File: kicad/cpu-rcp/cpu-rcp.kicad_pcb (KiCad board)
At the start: 2 copper layers, 86.4 x 63.5 mm, 79 parts, among them P1 RDRAM-EDGE, P5 NINTENDO-64_PINHEAD-25X2, SW1 Reset, U1 9480F, U10 CPU-NUS, U6 PIF-NUS, U7 MX8330, U9 RCP-NUS, X1 14.318MHz

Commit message: Work in progress, updated 3D shapes
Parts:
- added DA1: BAC54, n64:D_SOT-23_AAK, B.Cu at (96.5, 45.7)
- added FIL2: 3.3uH, n64:L_0805, B.Cu at (101.6, 47.0)
- added FIL4: 3.3uH, n64:L_0805, B.Cu at (101.6, 43.2)
- added JOY1: JOY OUT, n64:connector-molex-505110-0492, B.Cu at (105.9, 45.5)
- added R37: 750R, n64:R_0603, B.Cu at (92.0, 62.2)
- added R38: 750R, n64:R_0603, B.Cu at (85.1, 61.0)
- added U8: LC125, n64:ssop-14, B.Cu at (99.1, 58.4)
- moved U6 8.26 mm to (85.1, 52.1)
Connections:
- C144 pad 1: Net-(C144-Pad1) -> GND
- C144 pad 2: GND -> Net-(C144-Pad2)
- DCIN1 pad 4: ENABLE -> +3V3
- R36 pad 1: Net-(C144-Pad1) -> ENABLE
- R36 pad 2: ENABLE -> Net-(C144-Pad2)
- U6 pad 15: Net-(U6-Pad15) -> JOY1_DATA
- U6 pad 17: Net-(U6-Pad17) -> JOY2_DATA
- U7 pad 7: Net-(C144-Pad1) -> Net-(C144-Pad2)

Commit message: Laying around
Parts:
- C123, C127, C128, C5, C6, C7, C8, C9, CC1, CC2, CC3, CC4, CC5, CC6, CC7, CC8, CC9, CP1, CP2, CP3, CP4, CP5, CP6, CR1, CR10, CR11, CR12, CR13, CR14, CR15, CR2, CR3, CR4, CR5, CR6, CR7, CR8, CR9, CU1, CU7, CV1, CV2, R12, R13, R22, R23, R24, R28, R29, R3, R30, R34, R36, R4, SW1: moved to B.Cu
- moved SW1 60.5 mm to (36.8, 27.3), turned to 270 degrees
- moved AUDIO1 56.3 mm to (63.3, 83.5), turned to 0 degrees
- moved C127 54.1 mm to (42.5, 29.8)
- moved CR5 53.9 mm to (94.0, 45.7)
- moved C144 52.8 mm to (106.7, 73.7), turned to 270 degrees
- moved CR4 49.8 mm to (94.5, 52.7)
- moved CR3 48.1 mm to (94.6, 55.9)
- moved C40 47.6 mm to (102.2, 82.5), turned to 90 degrees
- moved C123 45.4 mm to (74.9, 41.9), turned to 180 degrees
- moved CC1 44.9 mm to (35.6, 41.9)
- moved CC5 42.2 mm to (43.2, 41.9)
- moved C128 42.2 mm to (62.9, 48.9), turned to 270 degrees
- moved CC2 40.3 mm to (35.6, 47.0)
- moved U1 38.7 mm to (64.1, 74.3)
- moved CR1 38.1 mm to (87.6, 63.5)
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
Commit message: Laying around
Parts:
- removed AUDIO1: AUDIO OUT, n64:connector-molex-505110-0492
- removed CP1, CP2, CP3, CP4, CP5, CP6, CV1, CV2: 100nF, n64:C_0603
- removed REF** (x4): MountingHole_3.2mm_M3, Mounting_Holes:MountingHole_3.2mm_M3_DIN965
- removed VDAC1: RCP DIGITAL RGB OUT, n64:connector-molex-505110-1092
- removed VIDEO1: VIDEO CLOCK/SYNC, n64:connector-molex-505110-0592
- added ANAUD1: ANALOG AUDIO OUT, n64:connector-molex-505110-0492, F.Cu at (64.1, 84.2)
- added AVSYNC1: VIDEO ENCODER SYNC, n64:connector-molex-505110-0492, F.Cu at (107.3, 35.6)
- added CU6: 100nF, n64:C_0603, B.Cu at (67.2, 29.2)
- added CU8: 100nF, n64:C_0603, B.Cu at (45.7, 36.8)
- added CVR1: 100nF, n64:C_0603, B.Cu at (81.3, 70.5)
- added CVR2: 100nF, n64:C_0603, B.Cu at (88.4, 71.1)
- added CVT1: 10uF, n64:C_1206, B.Cu at (90.2, 78.1)
- added CVT2: 100nF, n64:C_0603, B.Cu at (90.2, 74.9)
- added DVO1: DIGITAL VIDEO OUT, n64:connector-molex-505110-1092, F.Cu at (108.5, 54.1)
- C128, C142, C33, C73: footprint n64:CP_Tantalum_Case-D_EIA-7343-31_Reflow -> n64:C_1206
- JOY1: value JOY OUT -> GAMEPAD
- R12, R13, R36: moved to F.Cu
- moved R34 53.8 mm to (34.3, 33.0)
- moved JOY1 51.4 mm to (30.5, 29.8)
- moved R23 43.2 mm to (56.0, 26.7)
- moved R22 40.6 mm to (61.6, 26.7)
- moved R37 39.2 mm to (75.5, 26.7)
- moved R28 38.4 mm to (104.3, 34.9)
- moved SW1 34.9 mm to (71.8, 27.3)
- moved R38 34.3 mm to (91.4, 27.3)
- moved U8 32.6 mm to (40.6, 36.8), turned to 0 degrees
- moved R12 31.6 mm to (106.7, 78.1)
- moved R3 28.3 mm to (67.4, 37.5)
- moved R13 26.8 mm to (105.4, 64.1), turned to 90 degrees
- moved CR7 26.5 mm to (90.9, 40.0)
- moved R4 26.4 mm to (60.3, 44.5), turned to 270 degrees
- moved CR6 25.3 mm to (94.6, 43.8)
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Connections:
- P5 pad 13: Net-(P5-Pad13) -> (no net)
- P5 pad 38: Net-(P5-Pad38) -> (no net)
- U10 pad 18: Net-(U10-Pad18) -> (no net)
- U10 pad 65: Net-(U10-Pad65) -> (no net)
- U10 pad 74: Net-(U10-Pad74) -> (no net)
- U10 pad 95: Net-(U10-Pad95) -> (no net)
- U6 pad 26: Net-(U6-Pad26) -> (no net)
- U7 pad 3: Net-(U7-Pad3) -> (no net)

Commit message: Work in progress, laying around
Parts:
- moved U8 1.42 mm to (41.3, 35.6)
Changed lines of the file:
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@@
     (links 437)
     (no_connects 431)
-    (area 16.939279 22.98 114.935 102.125001)
+    (area 25.249999 25.249999 111.910001 89.050001)
     (thickness 1.6)
     (drawings 10)
@@
   )
   (module n64:ssop-14 (layer B.Cu)
-    (at 40.64 36.83)
+    (at 41.275 35.56)
     (fp_text reference U8 (at -3.81 -1.27 270) (layer B.SilkS)
       (effects (font (size 1.2065 1.2065) (thickness 0.1016)) (justify left bottom mirror))

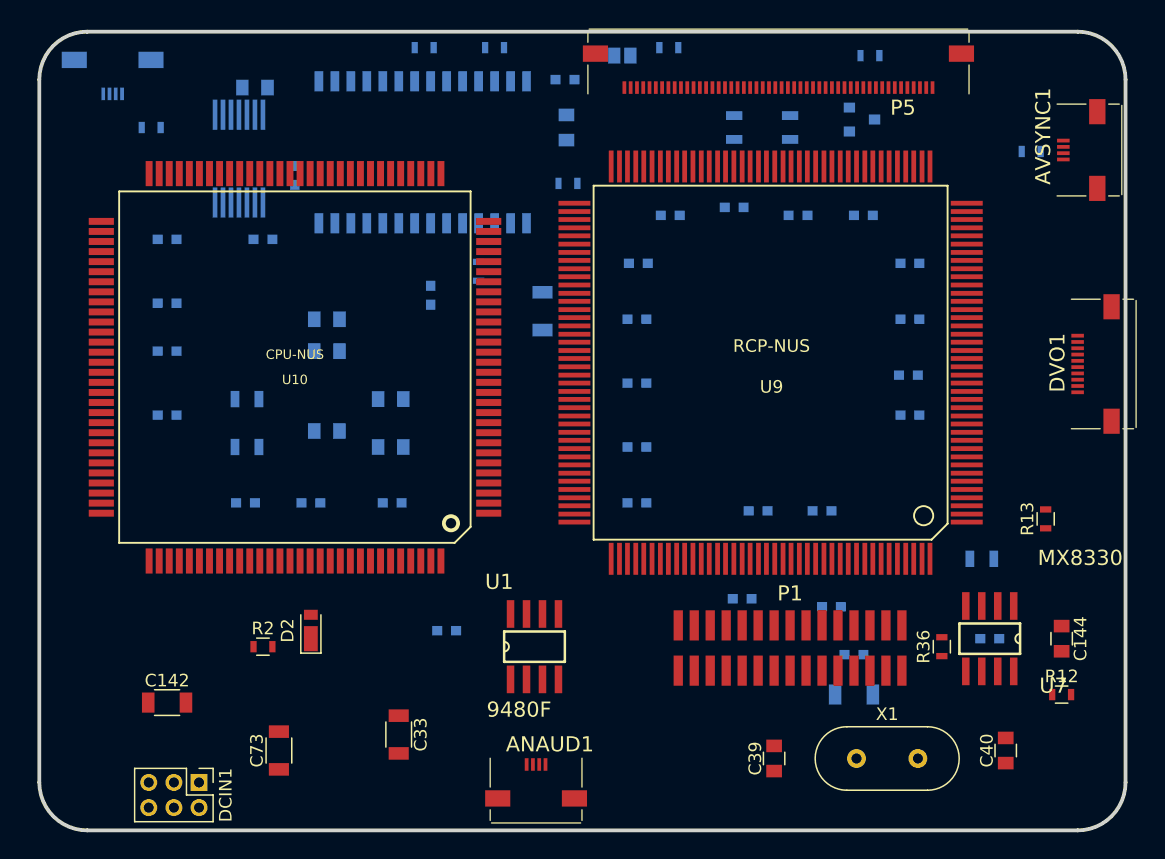
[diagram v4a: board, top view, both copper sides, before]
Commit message: Design Rules set according to my Fab House, switching to 4 layer board
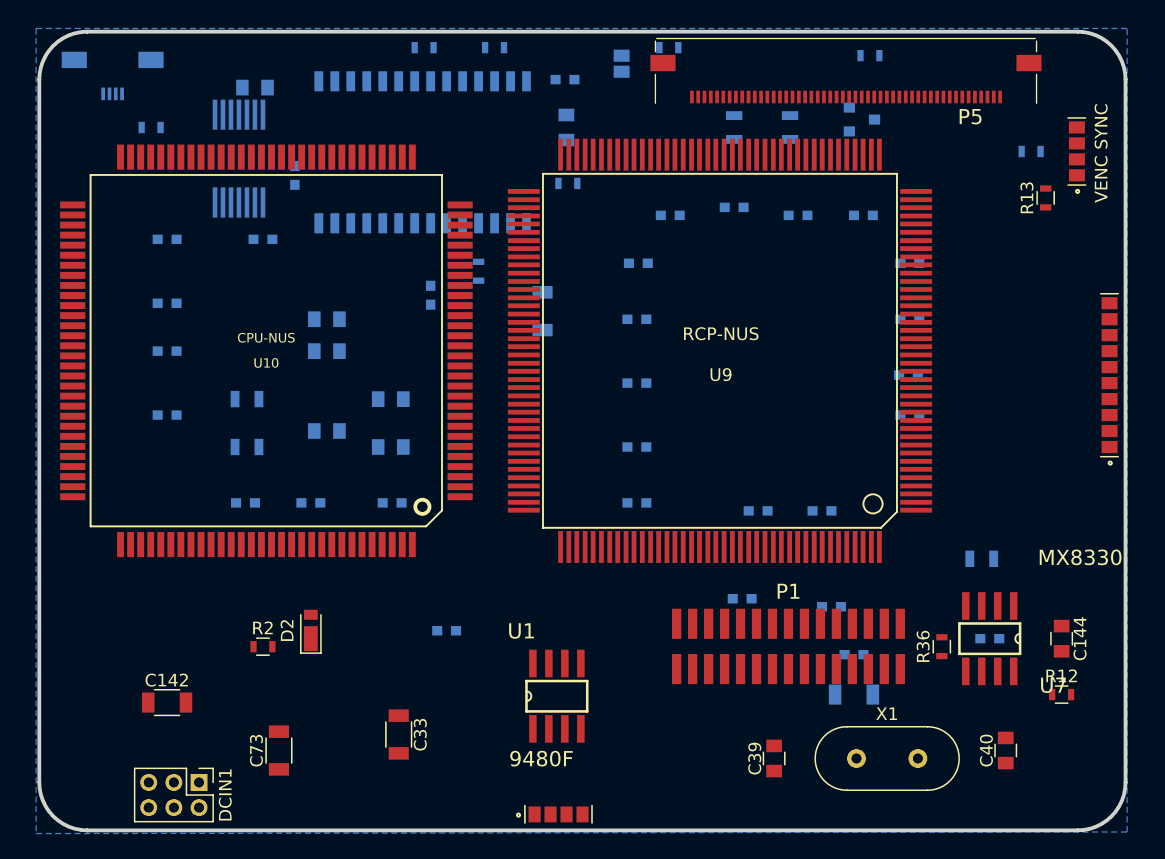
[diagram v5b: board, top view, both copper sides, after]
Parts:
- ANAUD1: value ANALOG AUDIO OUT -> AUDIO OUT; footprint n64:connector-molex-505110-0492 -> n64:Connectors_GS4
- AVSYNC1: value VIDEO ENCODER SYNC -> VENC SYNC; footprint n64:connector-molex-505110-0492 -> n64:Connectors_GS4
- DVO1: footprint n64:connector-molex-505110-1092 -> n64:Connectors_GS10
- moved R13 25.5 mm to (105.4, 38.6)
- moved P5 5.42 mm to (101.8, 30.1)
- moved DVO1 4.84 mm to (110.5, 58.4)
- moved U1 4.32 mm to (66.5, 78.2)
- moved U9 4.13 mm to (79.6, 50.7)
- moved ANAUD1 3.58 mm to (64.8, 87.7)
- moved U10 2.62 mm to (43.4, 50.8)
- moved AVSYNC1 1.42 mm to (108.0, 36.8)
- moved P1 0.18 mm to (75.7, 71.3)
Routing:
- added copper zone on B.Cu, net GND
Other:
- copper layers 2 -> 4
- net class Default: clearance 0.2 -> 0.15; trace_width 0.25 -> 0.15; via_dia 0.6 -> 0.3; via_drill 0.4 -> 0.2
- net class PWR added: clearance 0.3, trace_width 0.3, via_dia 0.6, via_drill 0.4
- rule trace_clearance: 0.2 -> 0.15
- rule trace_min: 0.2 -> 0.1
- rule via_min_drill: 0.3 -> 0.2
- rule via_min_size: 0.4 -> 0.2

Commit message: New Design Rules for my Fab, inner power layers added
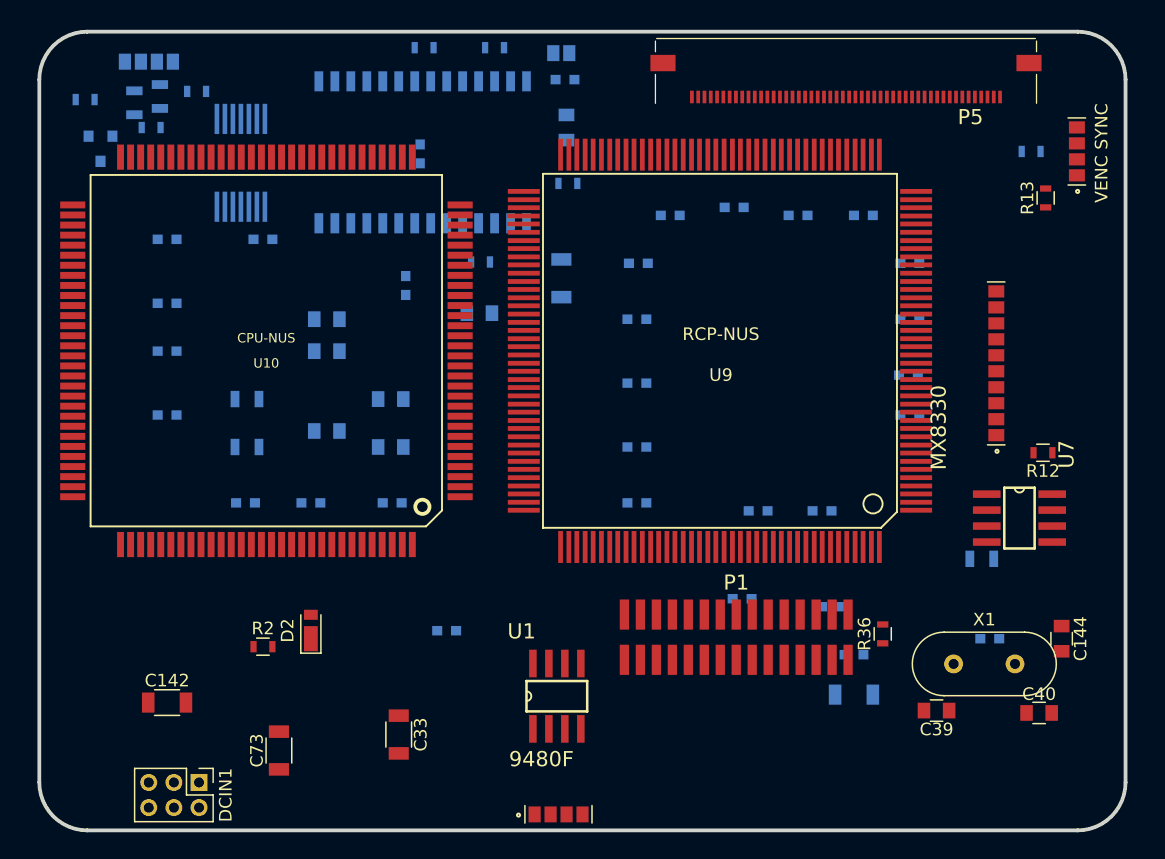
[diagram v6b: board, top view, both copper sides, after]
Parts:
- JOY1: footprint n64:connector-molex-505110-0492 -> n64:Connectors_GS4
- moved DA1 60.6 mm to (30.3, 34.7), turned to 270 degrees
- moved R38 53.6 mm to (37.9, 30.1)
- moved FIL2 50.2 mm to (35.0, 30.6)
- moved FIL4 47.7 mm to (33.0, 31.1)
- moved R37 46.6 mm to (29.0, 30.8)
- moved C127 25.3 mm to (60.4, 47.8)
- moved R12 19.3 mm to (105.2, 58.9), turned to 180 degrees
- moved C39 13.5 mm to (96.7, 79.4), turned to 180 degrees
- moved X1 10.8 mm to (98.1, 75.7)
- moved CU8 10.1 mm to (55.7, 35.1)
- moved U7 9.88 mm to (103.3, 64.1), turned to 270 degrees
- moved DVO1 9.05 mm to (101.5, 57.5)
- moved SW1 5.50 mm to (66.3, 27.1), turned to 0 degrees
- moved R36 4.81 mm to (92.5, 73.3)
- moved P1 4.22 mm to (71.5, 70.5)
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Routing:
- added copper zone on 3V3.Cu, net +3V3
- added copper zone on GND.Cu, net GND
- removed copper zone on B.Cu, net GND

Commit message: Caches updated
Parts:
- removed ANAUD1: AUDIO OUT, n64:Connectors_GS4
- removed AVSYNC1: VENC SYNC, n64:Connectors_GS4
- removed C33: 68uF, n64:C_1206
- removed R13: 4K3, n64:R_0603
- removed U1: 9480F, n64:so-8
- added DAUD1: DIGITAL AUDIO OUT, n64:Connectors_GS4, F.Cu at (101.7, 64.8)
- JOY1: footprint n64:Connectors_GS4 -> n64:connector-molex-505110-0492
- moved U7 49.7 mm to (54.6, 73.7), turned to 0 degrees
- moved C40 42.8 mm to (62.2, 76.2)
- moved R12 39.8 mm to (67.3, 71.1), turned to 270 degrees
- moved C39 36.2 mm to (62.2, 68.6)
- moved X1 33.7 mm to (64.6, 72.4), turned to 180 degrees
- moved R36 25.2 mm to (67.3, 74.9)
- moved C144 12.7 mm to (94.0, 73.7)
- moved DCIN1 6.48 mm to (39.4, 78.7)
- moved C73 6.35 mm to (44.5, 76.2)
- moved C142 3.81 mm to (35.6, 74.9)
- moved P5 3.54 mm to (98.4, 31.2)
- moved D2 3.49 mm to (47.0, 76.2)
- moved R2 2.62 mm to (40.6, 74.9)
- moved DVO1 0.93 mm to (101.6, 58.4)
- moved P1 0.80 mm to (72.0, 71.2)
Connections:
- P5 pad 24: /External connections/AUDIO_OUT_L -> (no net)
- P5 pad 49: /External connections/AUDIO_OUT_R -> (no net)

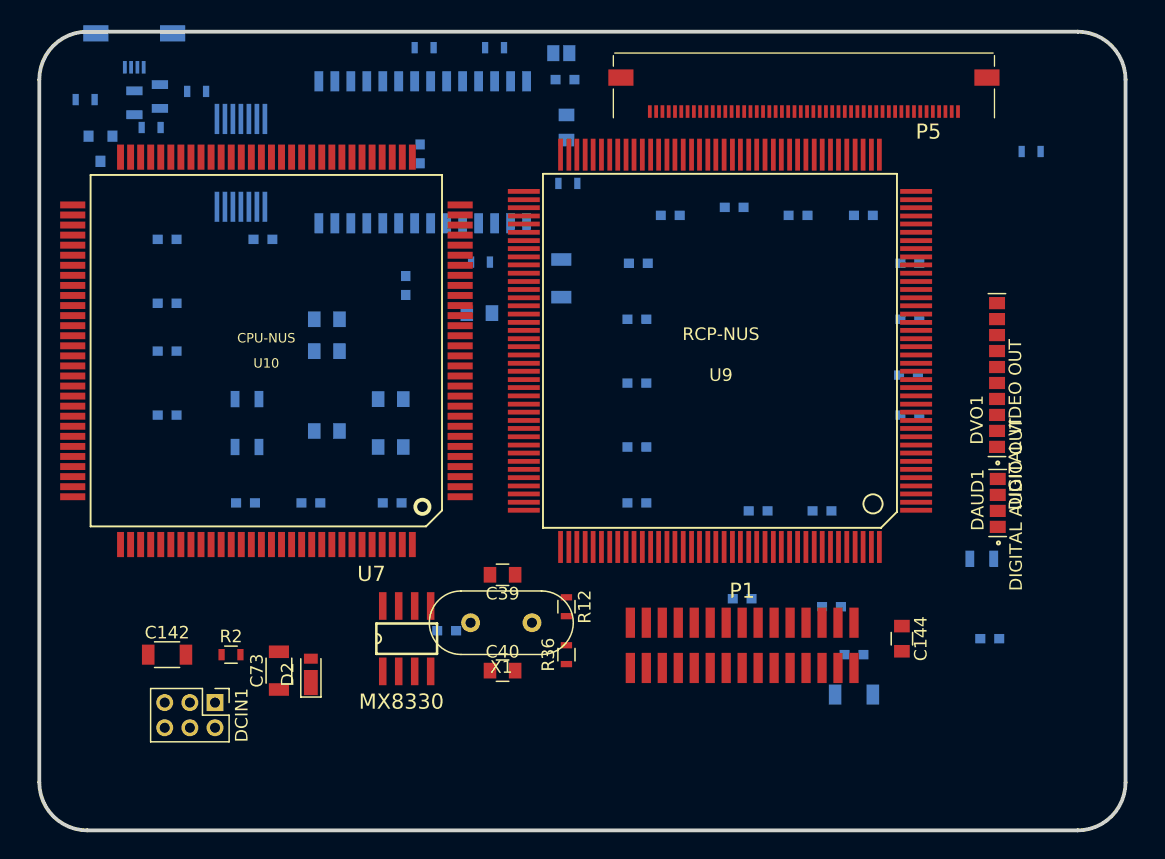
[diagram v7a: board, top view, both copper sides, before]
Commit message: Reduced board size and made slight changes to components layout
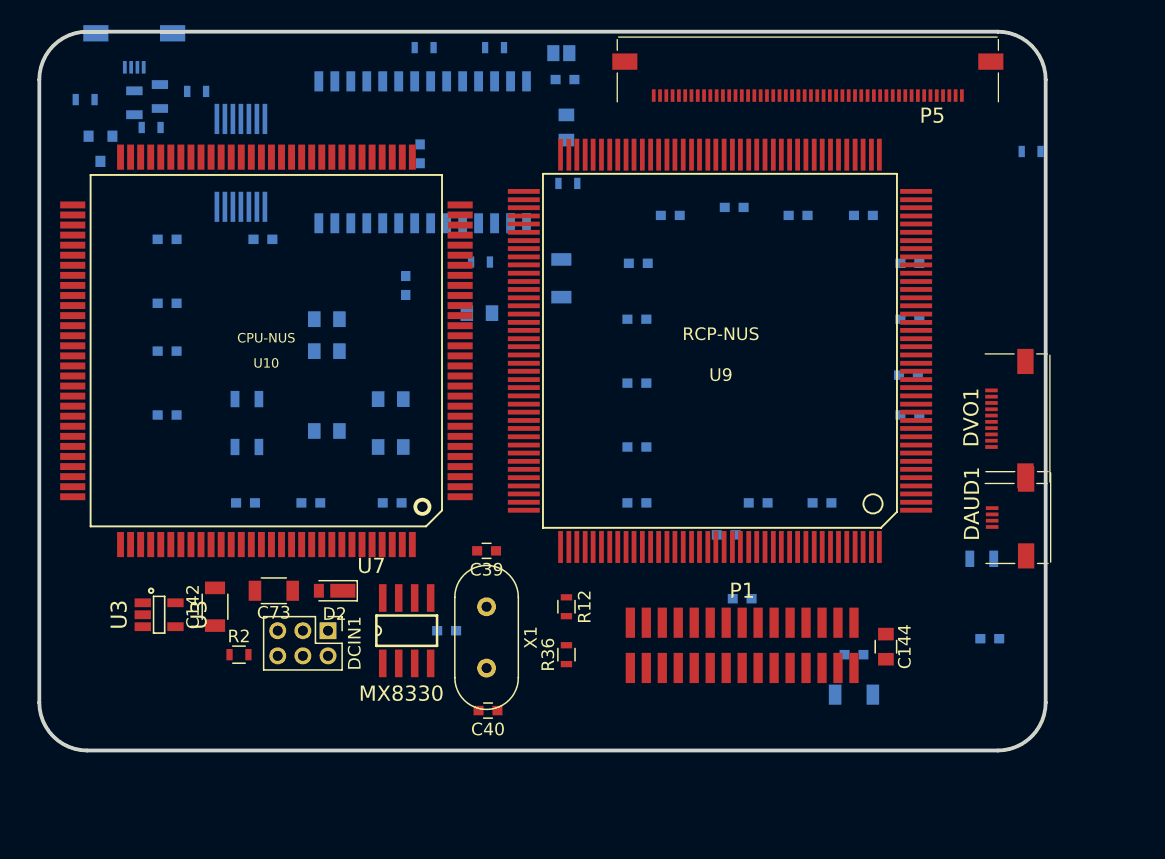
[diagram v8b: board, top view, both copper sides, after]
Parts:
- added U3: U3, n64:sot-23-5, F.Cu at (34.9, 71.8)
- C39, C40: footprint n64:C_0805 -> n64:C_0603
- DAUD1: footprint n64:Connectors_GS4 -> n64:connector-molex-505110-0492
- DVO1: footprint n64:Connectors_GS10 -> n64:connector-molex-505110-1092
- moved DCIN1 10.6 mm to (48.4, 73.0)
- moved CVR2 10.1 mm to (80.0, 65.4)
- moved D2 6.55 mm to (48.6, 69.8), turned to 180 degrees
- moved C73 6.36 mm to (44.0, 69.8), turned to 180 degrees
- moved C142 5.39 mm to (39.4, 71.1), turned to 90 degrees
- moved X1 3.83 mm to (61.0, 71.1), turned to 270 degrees
- moved C40 3.38 mm to (61.1, 79.4), turned to 180 degrees
- moved C39 2.29 mm to (61.0, 66.7)
- moved C144 1.42 mm to (92.7, 74.3)
- moved P5 1.31 mm to (98.8, 30.0)
- moved CR1 0.63 mm to (87.6, 62.9)
- moved CR2 0.63 mm to (82.5, 62.9)
- moved R2 0.63 mm to (41.3, 74.9)
- moved U7 0.63 mm to (54.6, 73.0)
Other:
- board size 86.4 x 63.5 mm -> 80 x 57.1 mm
